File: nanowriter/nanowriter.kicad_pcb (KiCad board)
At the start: 2 copper layers, 19 parts, among them IC1 ATMEGA32U2, J1 USB_mini_micro_B, K1 KEYSW, K2 KEYSW, K3 KEYSW, K4 KEYSW, K5 KEYSW, K6 KEYSW, SW1 SW_PUSH, X1 XTAL_GND

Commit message: Rev 1 pcb
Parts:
- removed C1, C2: 22p, Capacitors_SMD:C_0805_HandSoldering
- removed C3: 0.1u, Capacitors_SMD:C_0805_HandSoldering
- removed C4: 4.7u, Capacitors_SMD:C_0805_HandSoldering
- removed C5: 1u, Capacitors_SMD:C_0805_HandSoldering
- removed IC1: ATMEGA32U2, keyboard_parts:QFP32
- removed J1: USB_mini_micro_B, keyboard_parts:USB_microB
- removed R1, R2: 10k, Resistors_SMD:R_0805_HandSoldering
- removed R3, R4: 22, Resistors_SMD:R_0805_HandSoldering
- removed SW1: SW_PUSH, Buttons_Switches_SMD:SW_SPST_TL3342
- removed X1: XTAL_GND, keyboard_parts:FA-238
- added U1: ProMicro, keebs:Pro_Micro, B.Cu at (134.6, 96.5)
- K1, K2, K3, K4, K5, K6: footprint keebs:Mx_Alps_100 -> Keyboard:CHERRY_PCB_100H
- moved K2 37.9 mm to (153.7, 108.0)
- moved K3 37.9 mm to (153.7, 88.9)
- moved K5 37.9 mm to (115.6, 88.9)
- moved K6 37.9 mm to (96.5, 88.9)
- moved K1 37.9 mm to (134.6, 108.0)
- moved K4 37.9 mm to (134.6, 88.9)
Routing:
- net Net-(K2-Pad2): track 0.00 -> 69.4 mm
- net Net-(K5-Pad2): track 0.00 -> 48.2 mm
- net Net-(K6-Pad2): track 0.00 -> 36.9 mm
- net Net-(K3-Pad2): track 0.00 -> 27.2 mm
- net Net-(K4-Pad2): track 0.00 -> 26.3 mm
- net Net-(K1-Pad2): track 0.00 -> 16.8 mm
- added copper zone on B.Cu, net GND
- added copper zone on F.Cu, net GND
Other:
- board outline added: 74.9 x 36.8 mm
- board text added: "nanowriter.org"

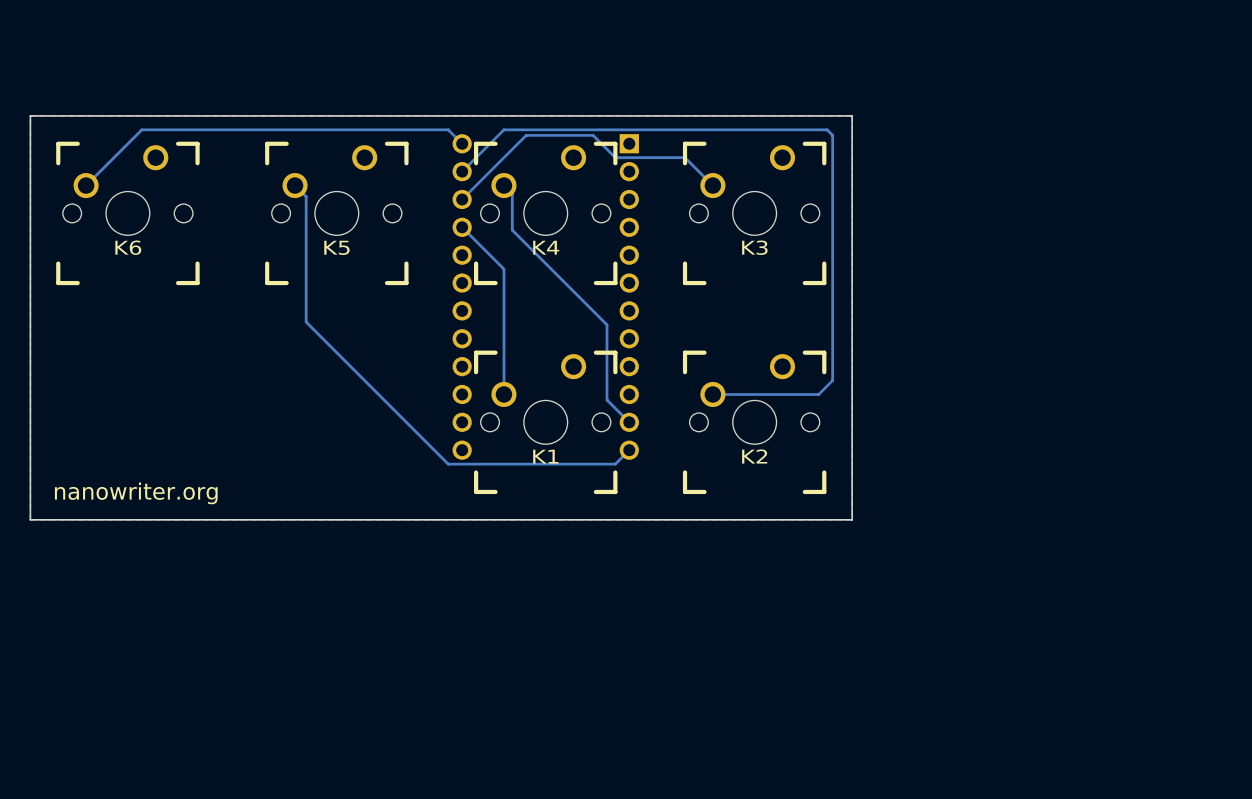
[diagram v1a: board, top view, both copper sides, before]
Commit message: Rev. 2 board
- Minimized dimension
- Added mounting holes
- Added reset switch with pullup
- Fixed pins 13-24 on pro-micro being backwards
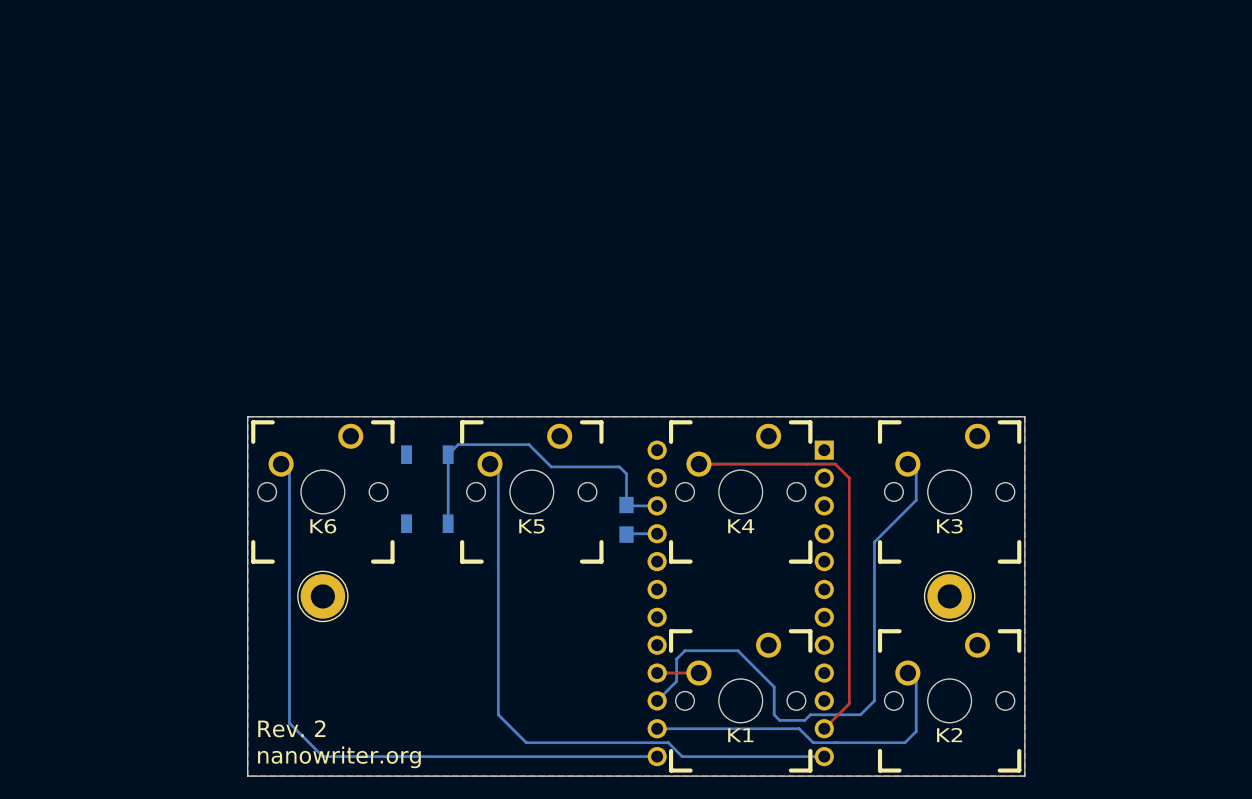
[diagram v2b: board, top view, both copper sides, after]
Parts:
- added R1: 10k, Resistors_SMD:R_0805_HandSoldering, B.Cu at (142.0, 116.8)
- added REF**: 1pin, Connectors:1pin, F.Cu at (114.3, 123.8)
- added REF**: 1pin, Connectors:1pin, F.Cu at (171.4, 123.8)
- added SW1: SW_PUSH, Buttons_Switches_SMD:SW_SPST_TL3342, B.Cu at (123.8, 114.0)
- moved U1 33.1 mm to (152.4, 124.5)
- moved K1 31.0 mm to (152.4, 133.3)
- moved K2 31.0 mm to (171.4, 133.3)
- moved K3 31.0 mm to (171.4, 114.3)
- moved K4 31.0 mm to (152.4, 114.3)
- moved K5 31.0 mm to (133.3, 114.3)
- moved K6 31.0 mm to (114.3, 114.3)
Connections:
- U1 pad 21: Net-(U1-Pad21) -> VCC
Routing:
- net Net-(K2-Pad2): track 69.4 -> 30.2 mm
- net Net-(R1-Pad1): track 0.00 -> 29.7 mm
- net Net-(K3-Pad2): track 27.2 -> 51.2 mm
- net Net-(K6-Pad2): track 36.9 -> 58.7 mm
- net Net-(K1-Pad2): track 16.8 -> 3.81 mm
- net Net-(K4-Pad2): track 26.3 -> 38.0 mm
- net Net-(K5-Pad2): track 48.2 -> 54.5 mm
- net VCC: track 0.00 -> 2.83 mm
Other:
- board size 74.9 x 36.8 mm -> 70.9 x 32.8 mm
- rule pad_to_mask_clearance: 0.2 -> 0
- board text added: "Rev. 2 nanowriter.org"
- board text removed: "nanowriter.org"

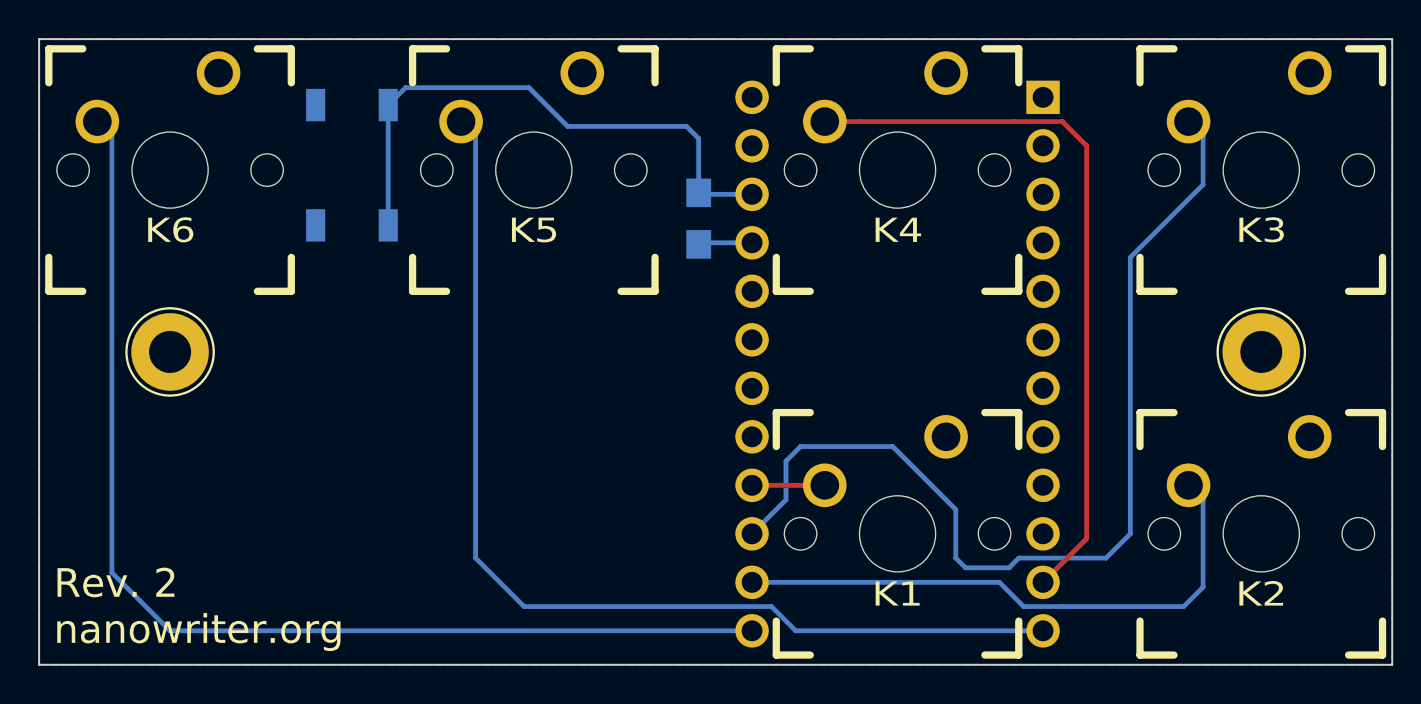
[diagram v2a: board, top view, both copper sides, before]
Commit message: PCB rev 3. Changed from Pro Micro based design to directly using an Atmega32u2
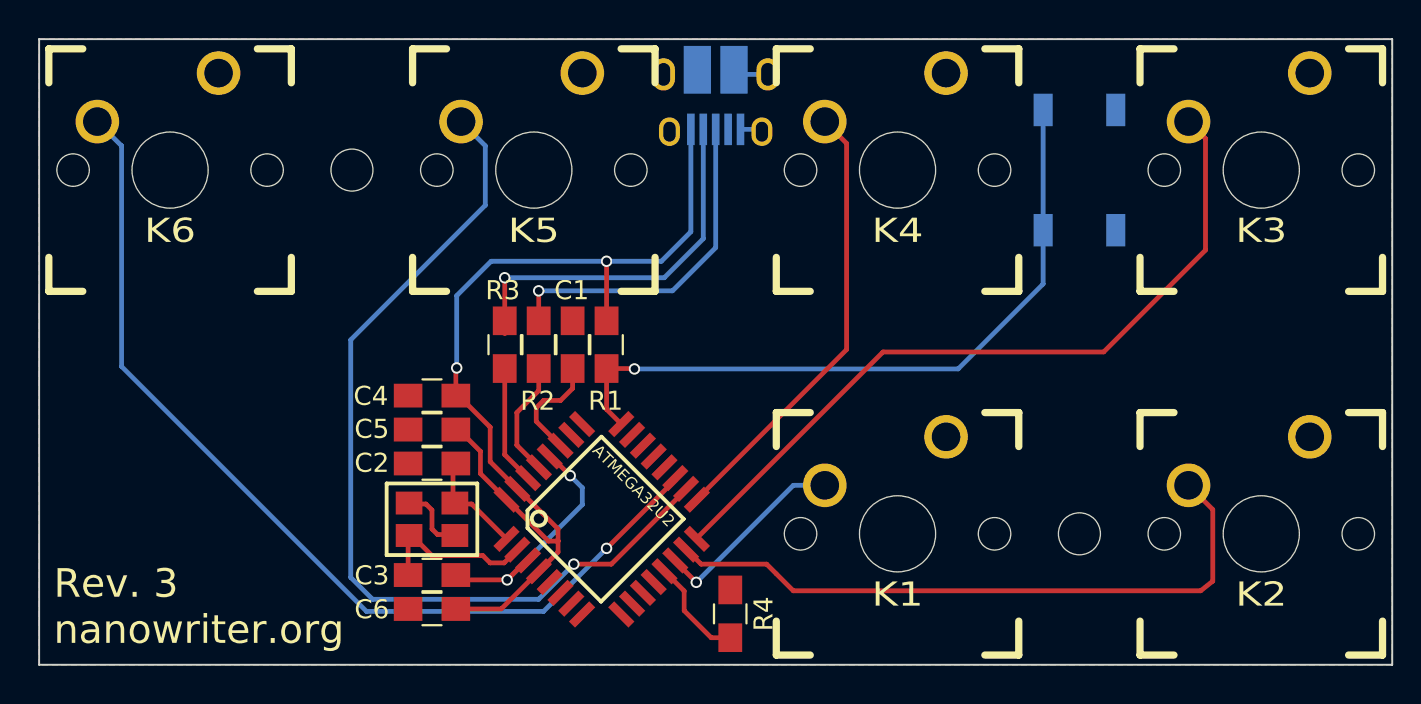
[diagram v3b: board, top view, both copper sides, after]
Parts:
- removed the REF** at (114.3, 123.8)
- removed the REF** at (171.4, 123.8)
- removed U1: ProMicro, keebs:Pro_Micro
- added C1: 1u, Capacitors_SMD:C_0805_HandSoldering, F.Cu at (135.4, 123.4)
- added C2: 22p, Capacitors_SMD:C_0805_HandSoldering, F.Cu at (128.0, 129.7)
- added C3: 22p, Capacitors_SMD:C_0805_HandSoldering, F.Cu at (128.0, 135.5)
- added C4: 4.7u, Capacitors_SMD:C_0805_HandSoldering, F.Cu at (128.0, 126.1)
- added C5: .1u, Capacitors_SMD:C_0805_HandSoldering, F.Cu at (128.0, 127.9)
- added C6: .1u, Capacitors_SMD:C_0805_HandSoldering, F.Cu at (128.0, 137.3)
- added IC1: ATMEGA32U2, keyboard_parts:QFP32, F.Cu at (136.9, 132.6)
- added R2: 22, Capacitors_SMD:C_0805_HandSoldering, F.Cu at (133.6, 123.4)
- added R3: 22, Capacitors_SMD:C_0805_HandSoldering, F.Cu at (131.8, 123.4)
- added R4: 10k, Capacitors_SMD:C_0805_HandSoldering, F.Cu at (143.6, 137.5)
- added REF**: MountingHole_2.2mm_M2, Mounting_Holes:MountingHole_2.2mm_M2, F.Cu at (123.8, 114.3)
- added REF**: MountingHole_2.2mm_M2, Mounting_Holes:MountingHole_2.2mm_M2, F.Cu at (161.9, 133.3)
- added USB: USB_mini_micro_B, Connectors:USB_Micro-B_10103594-0001LF, B.Cu at (142.9, 110.7)
- added X1: XTAL_GND, keyboard_parts:FA-238, F.Cu at (128.0, 132.6)
- K1, K2, K3, K4, K5, K6: footprint Keyboard:CHERRY_PCB_100H -> Keyboard:CHERRY_PLATE_100H
- R1: footprint Resistors_SMD:R_0805_HandSoldering -> Capacitors_SMD:C_0805_HandSoldering; moved to F.Cu
- moved SW1 38.1 mm to (161.9, 114.3), turned to 90 degrees
- moved R1 8.18 mm to (137.2, 123.4), turned to 90 degrees
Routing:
- net VCC: track 2.83 -> 52.9 mm, vias 0 -> 2
- net GND: track 0.00 -> 20.3 mm, vias 0 -> 2
- net Net-(J1-Pad2): track 0.00 -> 19.9 mm, vias 0 -> 1
- net Net-(J1-Pad3): track 0.00 -> 18.0 mm, vias 0 -> 1
- net Net-(IC1-Pad17): track 38.0 -> 23.5 mm
- net Net-(IC1-Pad16): track 51.2 -> 40.0 mm
- net Net-(C3-Pad1): track 0.00 -> 8.66 mm
- net Net-(IC1-Pad19): track 58.7 -> 50.7 mm, vias 0 -> 1
- net Net-(IC1-Pad24): track 29.7 -> 37.1 mm, vias 0 -> 1
- net Net-(IC1-Pad18): track 54.5 -> 47.8 mm, vias 0 -> 1
- net Net-(IC1-Pad14): track 3.81 -> 10.4 mm, vias 0 -> 1
- net Net-(IC1-Pad30): track 0.00 -> 6.25 mm
- net Net-(IC1-Pad29): track 0.00 -> 6.12 mm
- net Net-(C1-Pad1): track 0.00 -> 5.88 mm
- net Net-(C2-Pad1): track 0.00 -> 5.74 mm
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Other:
- board text added: "Rev. 3 nanowriter.org"
- board text removed: "Rev. 2 nanowriter.org"

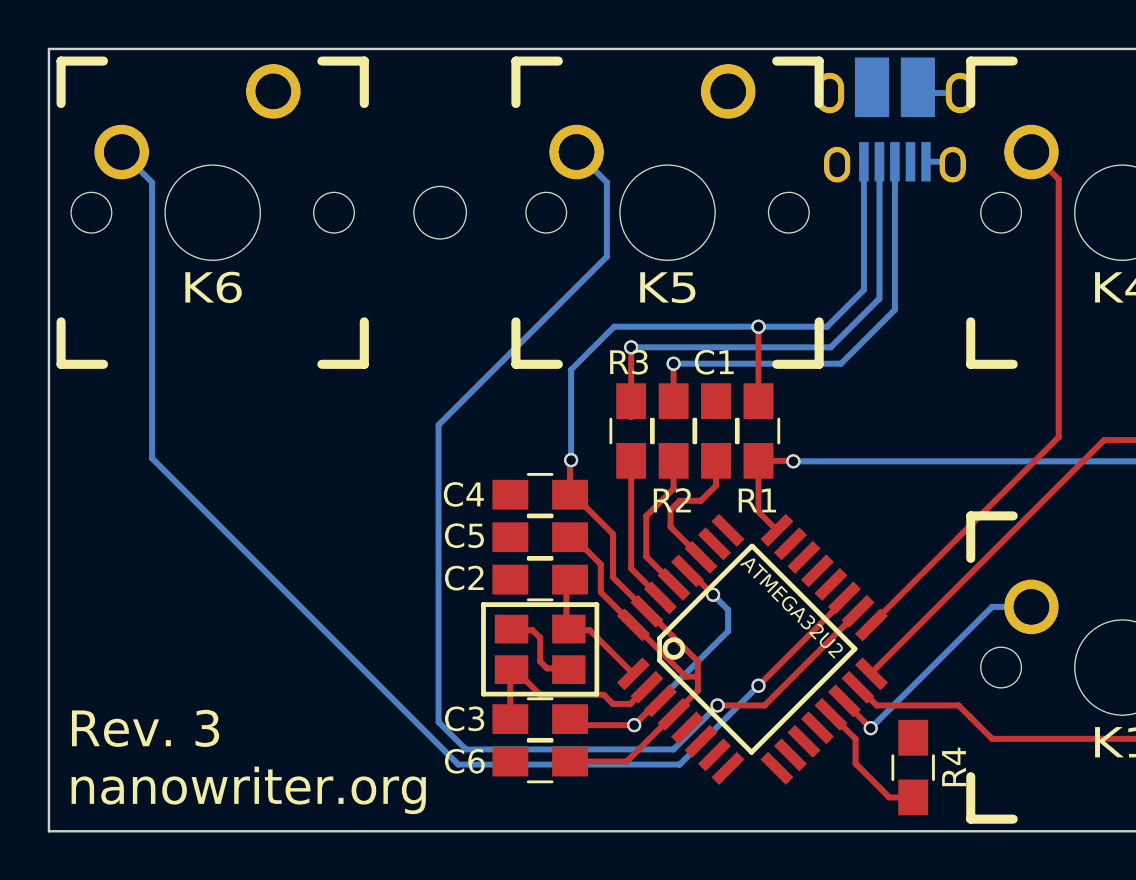
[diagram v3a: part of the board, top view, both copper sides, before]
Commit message: PCB rev 4. Changed to all smd usb port.
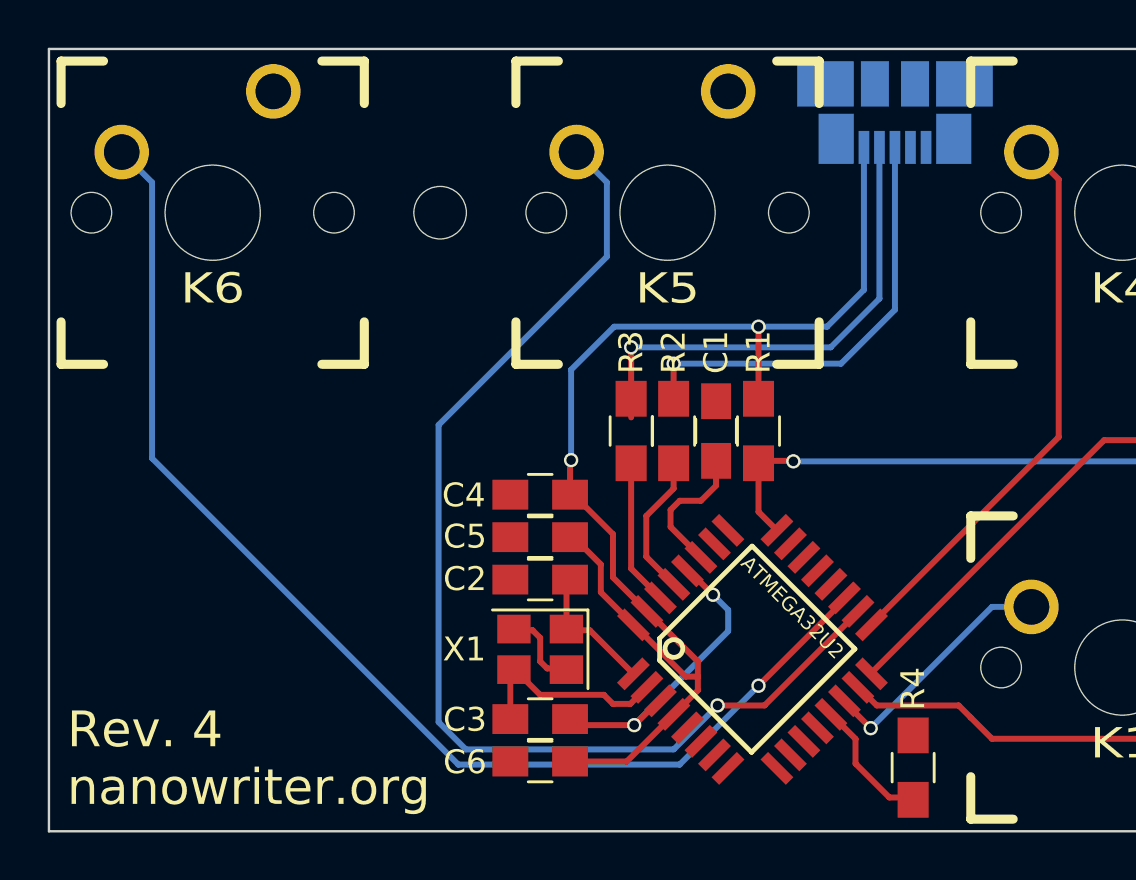
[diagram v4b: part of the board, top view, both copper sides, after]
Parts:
- removed USB: USB_mini_micro_B, Connectors:USB_Micro-B_10103594-0001LF
- added J1: USB, Connectors_Molex:USB_Micro-B_Molex_47346-0001, B.Cu at (142.9, 110.2)
- added REF***: OSHW-Symbol_6.7x6mm_SilkScreen, Symbols:OSHW-Symbol_6.7x6mm_SilkScreen, B.Cu at (142.9, 123.6)
- K1, K2, K3, K4, K5, K6: footprint Keyboard:CHERRY_PLATE_100H -> TheKeebrary:MX_PCB_100H
- R1, R2, R3, R4: footprint Capacitors_SMD:C_0805_HandSoldering -> Resistors_SMD:R_0805_HandSoldering
- SW1: value SW_PUSH -> RST
- X1: footprint keyboard_parts:FA-238 -> Crystals:Crystal_SMD_Abracon_ABM8G-4pin_3.2x2.5mm
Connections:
- X1 pad 3: GND -> Net-(X1-Pad3)
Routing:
- net GND: track 20.3 -> 13.2 mm
- net Net-(X1-Pad3): track 0.00 -> 1.77 mm
- net Net-(C3-Pad1): track 8.66 -> 10.3 mm
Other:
- board text added: "Rev. 4 nanowriter.org"
- board text removed: "Rev. 3 nanowriter.org"
